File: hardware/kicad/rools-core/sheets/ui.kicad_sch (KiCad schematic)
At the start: 0 parts

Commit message: Wire rools-core KiCad sheets with global labels and UI peripherals.
Migrate inter-sheet nets to global labels and flesh out UI, power, and
child-sheet power entry so net names align with pins.h for PCB routing.

Co-authored-by: Cursor <cursoragent@cursor.com>
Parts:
- added C1: 100nF, symbol Device:C
- added J1: ST7735_SPI, symbol Connector_Generic:Conn_01x08
- added R1, R2, R3, R4, R5, R6, R7: 10k, symbol Device:R
- added SW1: EC12E, symbol patch-eagle:ENCODER
- added SW2: EC12E, ES_Daisy_Patch_Rev8:VH1-147, symbol patch-eagle:ENCODER
- added SW3: SW_Push, symbol Switch:SW_Push
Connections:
- new net: R4.1, R6.1
- new net +3.3V: C1.1, J1.2 (VCC), R1.1, R2.1, R3.1, R5.1, R7.1
- new net BTN_CENTER: R7.2, SW3.1
- new net ENC_A_A: R1.2, SW1.A
- new net ENC_A_B: R2.2, SW1.B
- new net ENC_A_SW: R3.2, SW1.E (2)
- new net ENC_B_A: R4.2, SW2.A
- new net ENC_B_B: R5.2, SW2.B
- new net ENC_B_SW: R6.2, SW2.E (2)
- new net GND: C1.2, J1.1 (GND), SW1.C, SW1.D (1), SW2.C, SW2.D (1), SW3.2
- new net LCD_BLK: J1.8 (BLK)
- new net LCD_CS: J1.7 (CS)
- new net LCD_DC: J1.6 (DC)
- new net LCD_MOSI: J1.4 (MOSI)
- new net LCD_RST: J1.5 (RST)
- new net LCD_SCK: J1.3 (SCK)
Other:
- note added: "J1: GND VCC SCK MOSI RST DC CS BLK"

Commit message: Add QSPI settings persistence, CV calibration app, and CV output driver.
Co-authored-by: Cursor <cursoragent@cursor.com>
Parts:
- renumbered C1 to C20, R1 to R36, R2 to R37, R3 to R38, R4 to R39, R5 to R40, R6 to R41, R7 to R42
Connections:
- net +3.3V renamed +3V3_D

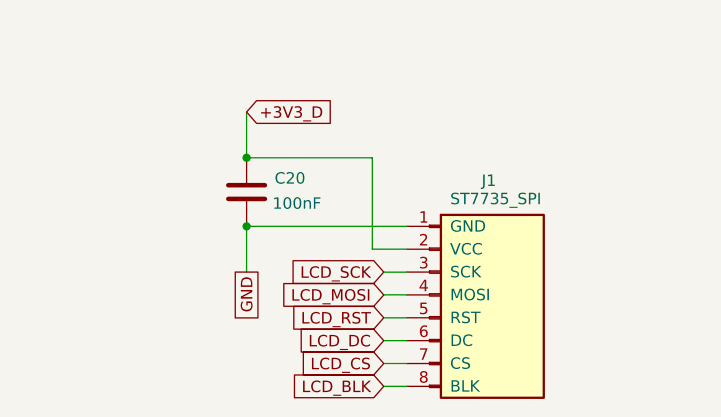
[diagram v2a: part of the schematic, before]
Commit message: Sync Core schematic Rev 0.2 with docs and firmware.
Align DAC8565/OPA4171 CV path (2.5V internal ref, 12.5k/100k), LM393 power-fail hold-up, and SPI1 CV driver fixes (LDAC polarity, debounced save with backlight off).

Co-authored-by: Cursor <cursoragent@cursor.com>
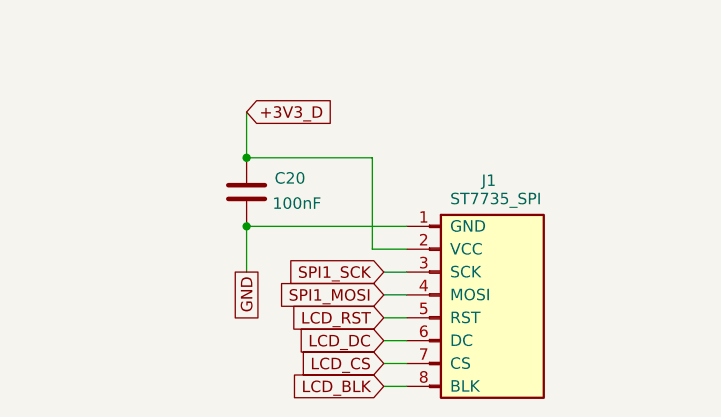
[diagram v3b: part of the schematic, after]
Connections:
- net LCD_MOSI renamed SPI1_MOSI
- net LCD_SCK renamed SPI1_SCK
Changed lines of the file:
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@@
 		)
 	)
-	(global_label "LCD_SCK"
+	(global_label "SPI1_SCK"
 		(shape input)
 		(at 66.04 114.3 180)
@@
 		)
 	)
-	(global_label "LCD_MOSI"
+	(global_label "SPI1_MOSI"
 		(shape input)
 		(at 66.04 116.84 180)

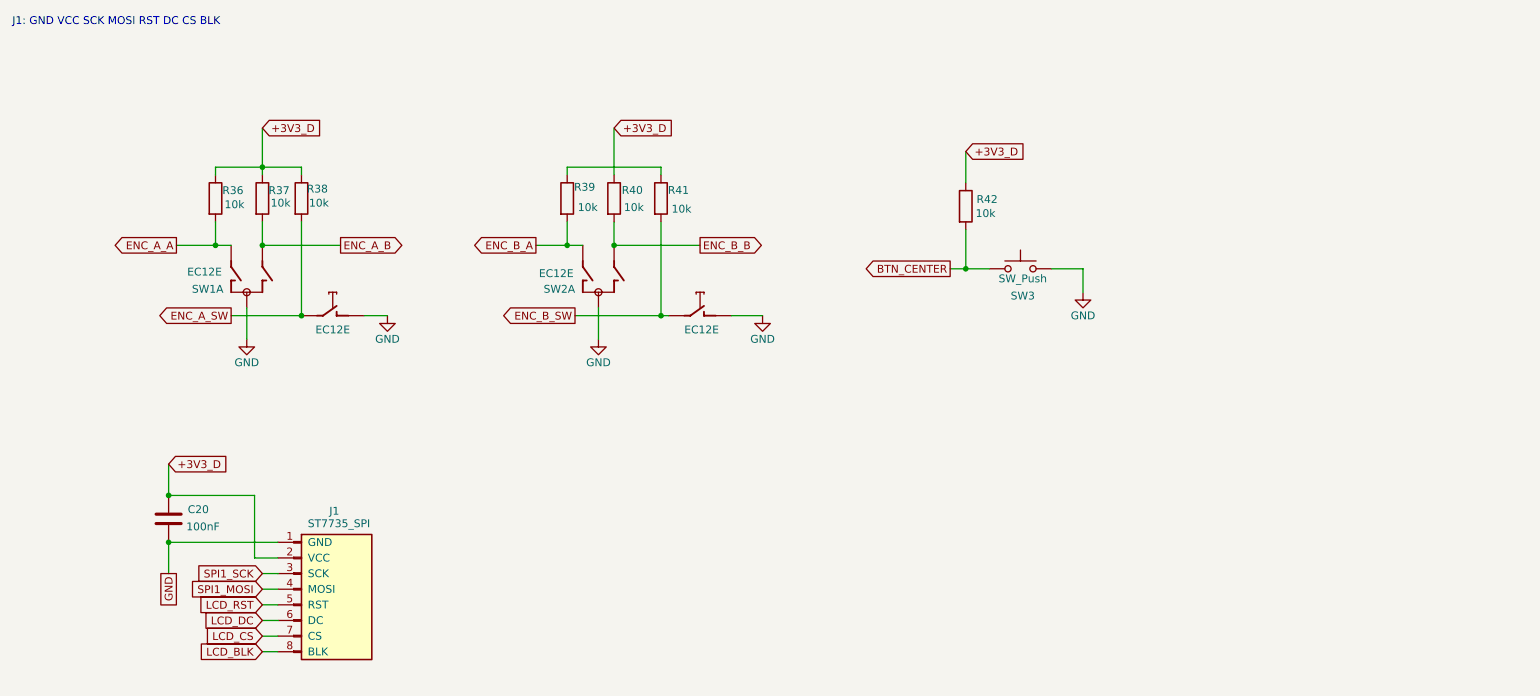
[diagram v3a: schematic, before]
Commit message: Finalize Core schematic pin map and JLC BOM for assembly.
MIDI USART1 on D13/D14, DAC8565 on D26/D27, and document P2 EXP_BUS so Exp I/O no longer conflicts with CV Out.

Co-authored-by: Cursor <cursoragent@cursor.com>
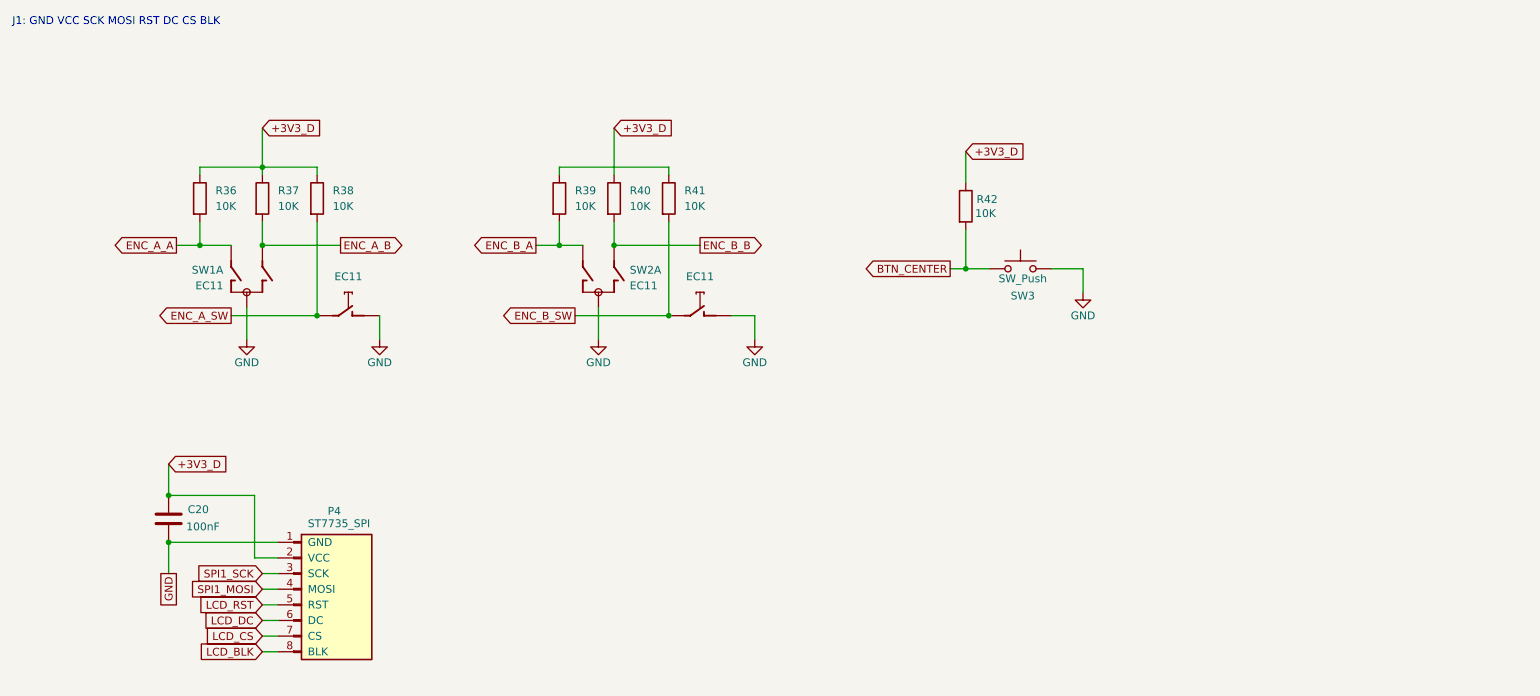
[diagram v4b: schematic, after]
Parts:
- C20: footprint (none) -> Capacitor_SMD:C_0603_1608Metric; LCSC (none) -> C14663
- P4: renamed from J1; footprint (none) -> Connector_PinHeader_2.54mm:PinHeader_1x08_P2.54mm_Vertical
- R36, R37, R38, R39, R40, R41, R42: value 10k -> 10K; footprint (none) -> Resistor_SMD:R_0603_1608Metric; LCSC (none) -> C25804
- SW1, SW2: value EC12E -> EC11; footprint (none) -> Rotary_Encoder:RotaryEncoder_Alps_EC11E-Switch_Vertical_H20mm
- SW1, SW2: value EC12E -> EC11; footprint ES_Daisy_Patch_Rev8:VH1-147 -> Rotary_Encoder:RotaryEncoder_Alps_EC11E-Switch_Vertical_H20mm
- SW3: footprint (none) -> Button_Switch_THT:SW_PUSH_6mm
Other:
- moved on the sheet: R36, R38, R39, R41

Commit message: Use Patch ENCODERNOSILK symbols for EC11 encoders on UI sheet.
Co-authored-by: Cursor <cursoragent@cursor.com>
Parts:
- added unit 3 of SW1
- added unit 4 of SW1
- added unit 4 of SW2
- added unit 3 of SW2
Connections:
- net GND: now also SW1.GND1 (G), SW1.GND2 (G), SW2.GND1 (G), SW2.GND2 (G)

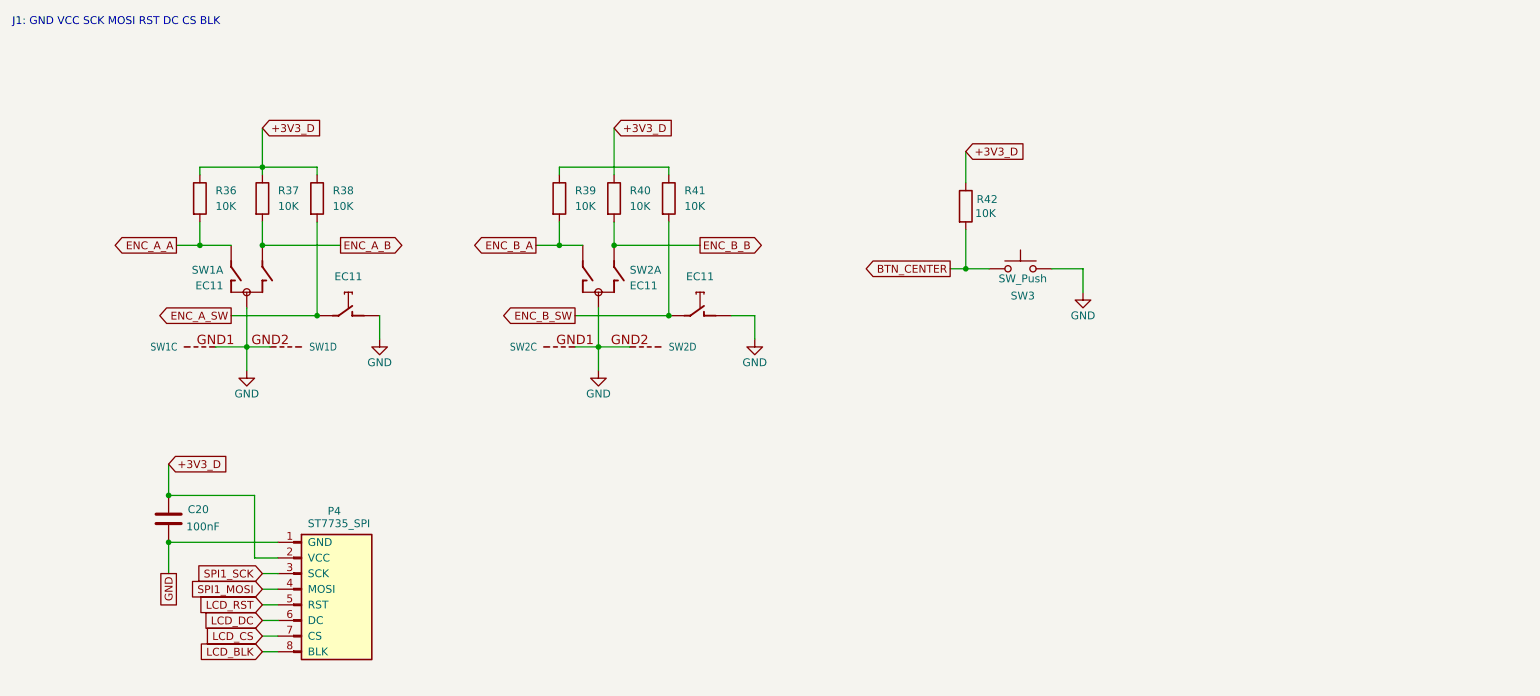
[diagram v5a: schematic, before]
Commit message: Lay out Core front-panel PCB for 10HP Eurorack fit.
Use RK09L 3-pin no-MP pots, split Daisy daughterboard, audio jack refs, and local display footprint library.

Co-authored-by: Cursor <cursoragent@cursor.com>
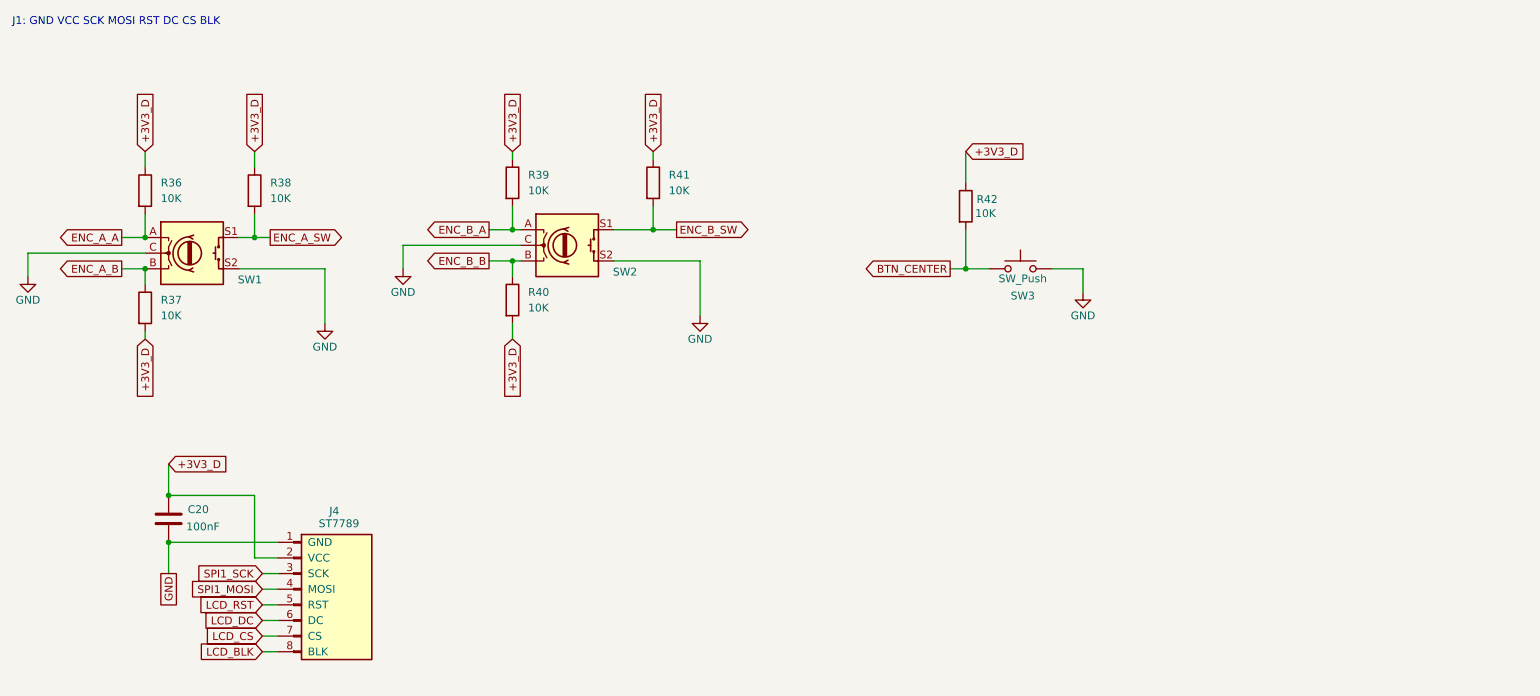
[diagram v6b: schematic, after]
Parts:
- removed unit 2 of SW1
- removed unit 3 of SW1
- removed unit 4 of SW1
- removed SW2: EC11, Rotary_Encoder:RotaryEncoder_Alps_EC11E-Switch_Vertical_H20mm, symbol patch-eagle:ENCODER
- added SW2: RotaryEncoder_Switch, Rotary_Encoder:RotaryEncoder_Alps_EC11E-Switch_Vertical_H20mm, symbol Device:RotaryEncoder_Switch
- J4: renamed from P4; value ST7735_SPI -> ST7789; footprint Connector_PinHeader_2.54mm:PinHeader_1x08_P2.54mm_Vertical -> Library:Display_1.54in_240x240
- SW1: value EC11 -> RotaryEncoder_Switch; symbol patch-eagle:ENCODER -> Device:RotaryEncoder_Switch
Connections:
- net +3V3_D: now also R37.2, R39.1, R40.2, R41.1; no longer R37.1, R40.1
- net ENC_A_B: now also R37.1; no longer R37.2
- net ENC_A_SW: now also SW1.S1
- net ENC_B_A: now also SW2.A
- net ENC_B_B: now also R40.1, SW2.B; no longer R40.2
- net ENC_B_SW: now also SW2.S1
- net GND: now also SW1.S2, SW2.C, SW2.S2
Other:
- moved on the sheet: R36, R37, R38, R39, R40, R41

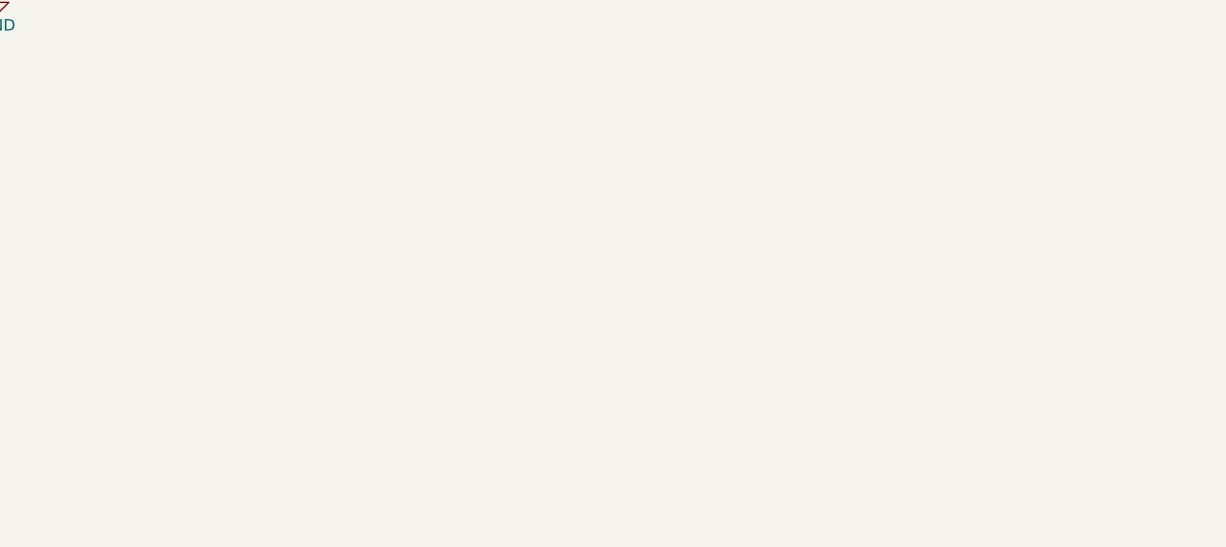
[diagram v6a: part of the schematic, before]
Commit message: Route Core PCB and place Daisy Seed on the daughterboard.
Sync schematic sheets with the split-board layout and updated interconnects.

Co-authored-by: Cursor <cursoragent@cursor.com>
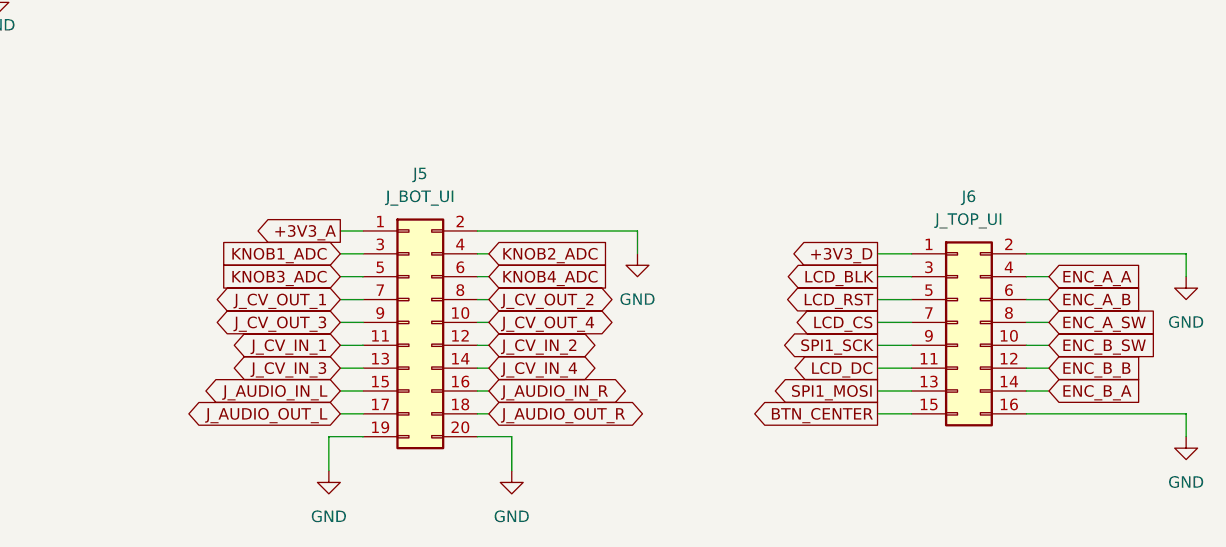
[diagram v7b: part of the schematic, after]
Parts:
- added J5: J_BOT_UI, Connector_PinHeader_2.54mm:PinHeader_2x10_P2.54mm_Vertical_SMD, symbol Connector_Generic:Conn_02x10_Odd_Even
- added J6: J_TOP_UI, Connector_PinHeader_2.54mm:PinHeader_2x08_P2.54mm_Vertical_SMD, symbol Connector_Generic:Conn_02x08_Odd_Even
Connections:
- net +3V3_D: now also J6.1 (Pin_1)
- net BTN_CENTER: now also J6.15 (Pin_15)
- net ENC_A_A: now also J6.4 (Pin_4)
- net ENC_A_B: now also J6.6 (Pin_6)
- net ENC_A_SW: now also J6.8 (Pin_8)
- net ENC_B_A: now also J6.14 (Pin_14)
- net ENC_B_B: now also J6.12 (Pin_12)
- net ENC_B_SW: now also J6.10 (Pin_10)
- net GND: now also J5.19 (Pin_19), J5.2 (Pin_2), J5.20 (Pin_20), J6.16 (Pin_16), J6.2 (Pin_2)
- net LCD_BLK: now also J6.3 (Pin_3)
- net LCD_CS: now also J6.7 (Pin_7)
- net LCD_DC: now also J6.11 (Pin_11)
- net LCD_RST: now also J6.5 (Pin_5)
- net SPI1_MOSI: now also J6.13 (Pin_13)
- net SPI1_SCK: now also J6.9 (Pin_9)
- new net +3V3_A: J5.1 (Pin_1)
- new net J_AUDIO_IN_L: J5.15 (Pin_15)
- new net J_AUDIO_IN_R: J5.16 (Pin_16)
- new net J_AUDIO_OUT_L: J5.17 (Pin_17)
- new net J_AUDIO_OUT_R: J5.18 (Pin_18)
- new net J_CV_IN_1: J5.11 (Pin_11)
- new net J_CV_IN_2: J5.12 (Pin_12)
- new net J_CV_IN_3: J5.13 (Pin_13)
- new net J_CV_IN_4: J5.14 (Pin_14)
- new net J_CV_OUT_1: J5.7 (Pin_7)
- new net J_CV_OUT_2: J5.8 (Pin_8)
- new net J_CV_OUT_3: J5.9 (Pin_9)
- new net J_CV_OUT_4: J5.10 (Pin_10)
- new net KNOB1_ADC: J5.3 (Pin_3)
- new net KNOB2_ADC: J5.4 (Pin_4)
- new net KNOB3_ADC: J5.5 (Pin_5)
- new net KNOB4_ADC: J5.6 (Pin_6)

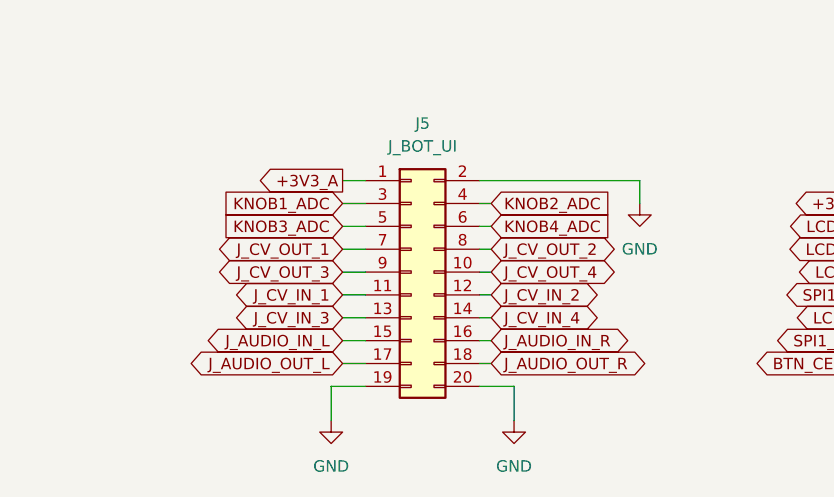
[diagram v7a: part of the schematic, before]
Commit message: Remove Patch reference assets and continue Core PCB routing.
Drop imported Patch symbols, local display footprint, and stale BOM CSV while advancing layout and schematic interconnects.

Co-authored-by: Cursor <cursoragent@cursor.com>
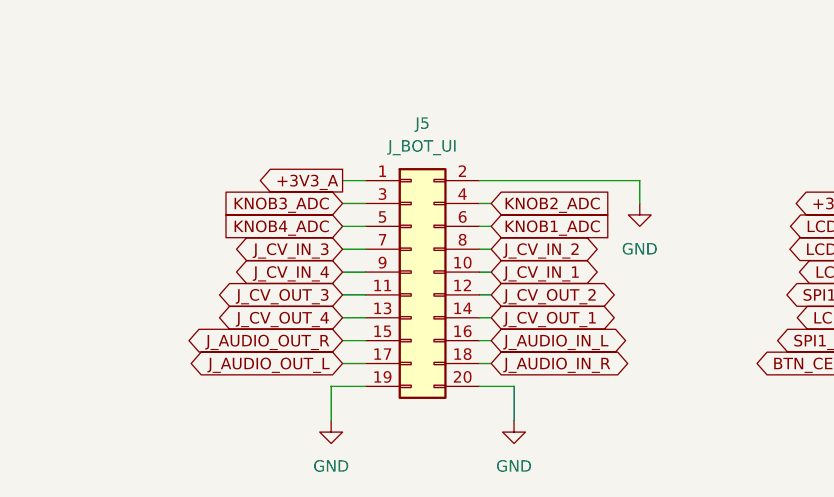
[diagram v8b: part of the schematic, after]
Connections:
- net J_AUDIO_IN_L: now also J5.16 (Pin_16); no longer J5.15 (Pin_15)
- net J_AUDIO_IN_R: now also J5.18 (Pin_18); no longer J5.16 (Pin_16)
- net J_AUDIO_OUT_R: now also J5.15 (Pin_15); no longer J5.18 (Pin_18)
- net J_CV_IN_1: now also J5.10 (Pin_10); no longer J5.11 (Pin_11)
- net J_CV_IN_2: now also J5.8 (Pin_8); no longer J5.12 (Pin_12)
- net J_CV_IN_3: now also J5.7 (Pin_7); no longer J5.13 (Pin_13)
- net J_CV_IN_4: now also J5.9 (Pin_9); no longer J5.14 (Pin_14)
- net J_CV_OUT_1: now also J5.14 (Pin_14); no longer J5.7 (Pin_7)
- net J_CV_OUT_2: now also J5.12 (Pin_12); no longer J5.8 (Pin_8)
- net J_CV_OUT_3: now also J5.11 (Pin_11); no longer J5.9 (Pin_9)
- net J_CV_OUT_4: now also J5.13 (Pin_13); no longer J5.10 (Pin_10)
- net KNOB1_ADC: now also J5.6 (Pin_6); no longer J5.3 (Pin_3)
- net KNOB3_ADC: now also J5.3 (Pin_3); no longer J5.5 (Pin_5)
- net KNOB4_ADC: now also J5.5 (Pin_5); no longer J5.6 (Pin_6)
